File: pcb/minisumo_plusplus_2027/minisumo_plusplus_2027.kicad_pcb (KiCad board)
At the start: 2 copper layers, 45 x 33 mm, 13 parts, among them J1 IR - Conn_01x03_Pin, J2 IR - Conn_01x03_Pin, J3 Start Module - Conn_01x04_Pin, J4 US - Conn_01x04_Pin, SW1 SW_SPDT, U3 ESP32-C6-SuperMini

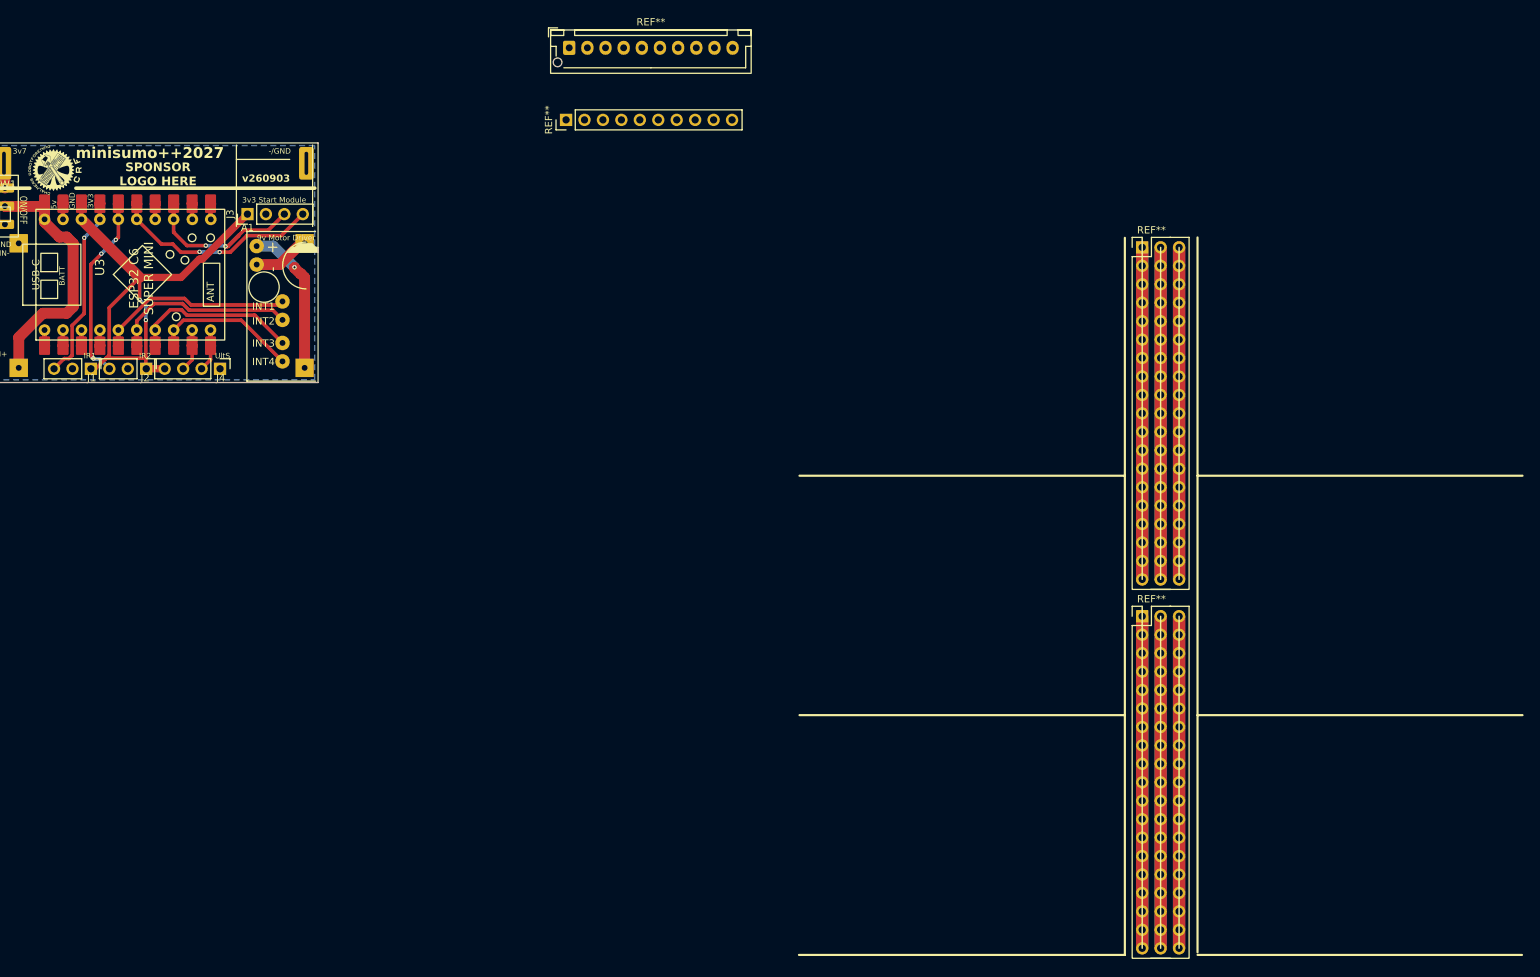
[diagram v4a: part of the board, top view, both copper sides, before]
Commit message: pcb - 1x10 for ir front/back and ultrasonic instead of 2x 1x3 + 1x4 && also included a 6x fab board example of latest board
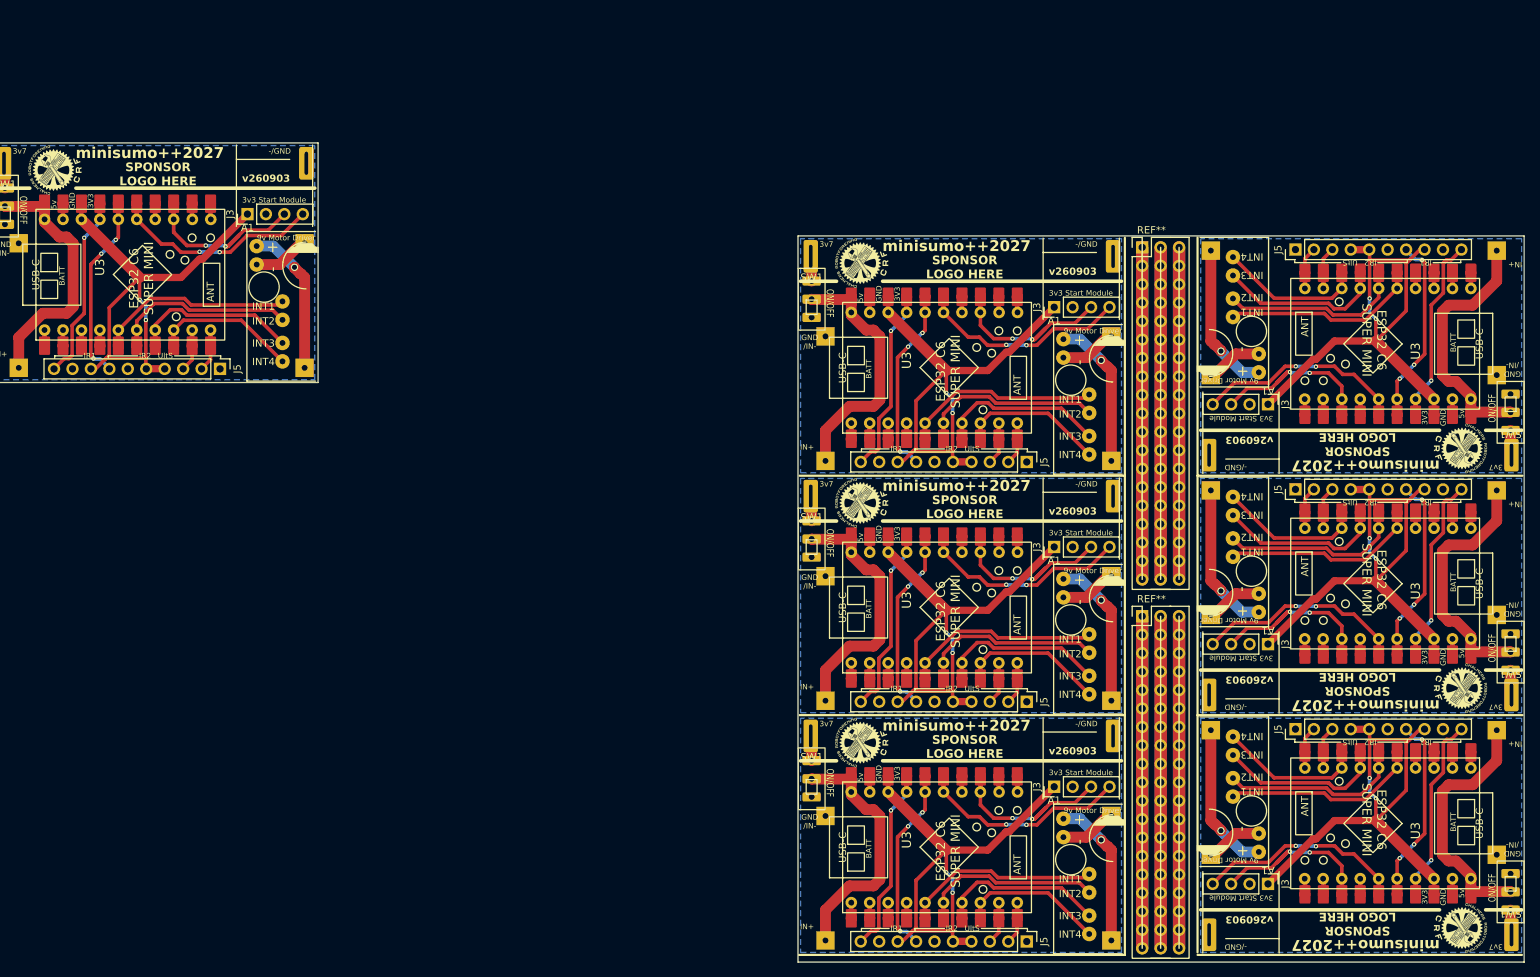
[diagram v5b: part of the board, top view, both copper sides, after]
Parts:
- removed J1, J2: IR - Conn_01x03_Pin, Connector_PinHeader_2.54mm:PinHeader_1x03_P2.54mm_Vertical
- removed J4: US - Conn_01x04_Pin, Connector_PinHeader_2.54mm:PinHeader_1x04_P2.54mm_Vertical
- removed the REF** at (108.4, 22.1)
- removed the REF** at (108.0, 32.0)
- added A1: ~, minisumo_plusplus_2027:Mini_L298N_2_Channel_H_Bridge_DC_Motor_Driver_Board_with_MX1508-special_silk, F.Cu at (175.2, 60.2)
- added A1: ~, minisumo_plusplus_2027:Mini_L298N_2_Channel_H_Bridge_DC_Motor_Driver_Board_with_MX1508-special_silk, F.Cu at (204.7, 101.8)
- added A1: ~, minisumo_plusplus_2027:Mini_L298N_2_Channel_H_Bridge_DC_Motor_Driver_Board_with_MX1508-special_silk, F.Cu at (175.2, 126.2)
- added A1: ~, minisumo_plusplus_2027:Mini_L298N_2_Channel_H_Bridge_DC_Motor_Driver_Board_with_MX1508-special_silk, F.Cu at (175.2, 93.2)
- added A1: ~, minisumo_plusplus_2027:Mini_L298N_2_Channel_H_Bridge_DC_Motor_Driver_Board_with_MX1508-special_silk, F.Cu at (204.7, 134.9)
- added A1: ~, minisumo_plusplus_2027:Mini_L298N_2_Channel_H_Bridge_DC_Motor_Driver_Board_with_MX1508-special_silk, F.Cu at (204.7, 68.8)
- added A2: ~, minisumo_plusplus_2027:XL6009 4A Boost Converter Step Up Adjustable 15W 5-32V to 5-50V DC-DC Power Supply Module LM2577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, B.Cu at (238.1, 81.1)
- added A2: ~, minisumo_plusplus_2027:XL6009 4A Boost Converter Step Up Adjustable 15W 5-32V to 5-50V DC-DC Power Supply Module LM2577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, B.Cu at (141.8, 80.9)
- added A2: ~, minisumo_plusplus_2027:XL6009 4A Boost Converter Step Up Adjustable 15W 5-32V to 5-50V DC-DC Power Supply Module LM2577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, B.Cu at (238.1, 48.1)
- added A2: ~, minisumo_plusplus_2027:XL6009 4A Boost Converter Step Up Adjustable 15W 5-32V to 5-50V DC-DC Power Supply Module LM2577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, B.Cu at (238.1, 114.2)
- added A2: ~, minisumo_plusplus_2027:XL6009 4A Boost Converter Step Up Adjustable 15W 5-32V to 5-50V DC-DC Power Supply Module LM2577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, B.Cu at (141.8, 146.9)
- added A2: ~, minisumo_plusplus_2027:XL6009 4A Boost Converter Step Up Adjustable 15W 5-32V to 5-50V DC-DC Power Supply Module LM2577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, B.Cu at (141.8, 113.9)
- added J3: Start Module - Conn_01x04_Pin, Connector_PinHeader_2.54mm:PinHeader_1x04_P2.54mm_Vertical, F.Cu at (204.7, 137.2)
- added J3: Start Module - Conn_01x04_Pin, Connector_PinHeader_2.54mm:PinHeader_1x04_P2.54mm_Vertical, F.Cu at (204.7, 104.2)
- added J3: Start Module - Conn_01x04_Pin, Connector_PinHeader_2.54mm:PinHeader_1x04_P2.54mm_Vertical, F.Cu at (204.7, 71.2)
- added J3: Start Module - Conn_01x04_Pin, Connector_PinHeader_2.54mm:PinHeader_1x04_P2.54mm_Vertical, F.Cu at (175.2, 123.9)
- added J3: Start Module - Conn_01x04_Pin, Connector_PinHeader_2.54mm:PinHeader_1x04_P2.54mm_Vertical, F.Cu at (175.2, 90.8)
- added J3: Start Module - Conn_01x04_Pin, Connector_PinHeader_2.54mm:PinHeader_1x04_P2.54mm_Vertical, F.Cu at (175.2, 57.8)
- added J5: Conn_01x10_Pin, Connector_PinHeader_2.54mm:PinHeader_1x10_P2.54mm_Vertical, F.Cu at (171.5, 112.1)
- added J5: Conn_01x10_Pin, Connector_PinHeader_2.54mm:PinHeader_1x10_P2.54mm_Vertical, F.Cu at (171.5, 79.1)
- added J5: Conn_01x10_Pin, Connector_PinHeader_2.54mm:PinHeader_1x10_P2.54mm_Vertical, F.Cu at (208.5, 49.9)
- added J5: Conn_01x10_Pin, Connector_PinHeader_2.54mm:PinHeader_1x10_P2.54mm_Vertical, F.Cu at (208.5, 115.9)
- added J5: Conn_01x10_Pin, Connector_PinHeader_2.54mm:PinHeader_1x10_P2.54mm_Vertical, F.Cu at (208.5, 82.9)
- added J5: Conn_01x10_Pin, Connector_PinHeader_2.54mm:PinHeader_1x10_P2.54mm_Vertical, F.Cu at (60.4, 66.3)
- added J5: Conn_01x10_Pin, Connector_PinHeader_2.54mm:PinHeader_1x10_P2.54mm_Vertical, F.Cu at (171.5, 145.2)
- added SW1: SW_SPDT, minisumo_plusplus_2027:SPST_switch_SS-12D00G4_1P2T_2.5mm_pitch_vert, F.Cu at (238.1, 74.8)
- added SW1: SW_SPDT, minisumo_plusplus_2027:SPST_switch_SS-12D00G4_1P2T_2.5mm_pitch_vert, F.Cu at (141.8, 87.2)
- added SW1: SW_SPDT, minisumo_plusplus_2027:SPST_switch_SS-12D00G4_1P2T_2.5mm_pitch_vert, F.Cu at (141.8, 54.2)
- added SW1: SW_SPDT, minisumo_plusplus_2027:SPST_switch_SS-12D00G4_1P2T_2.5mm_pitch_vert, F.Cu at (238.1, 140.8)
- added SW1: SW_SPDT, minisumo_plusplus_2027:SPST_switch_SS-12D00G4_1P2T_2.5mm_pitch_vert, F.Cu at (238.1, 107.8)
- added SW1: SW_SPDT, minisumo_plusplus_2027:SPST_switch_SS-12D00G4_1P2T_2.5mm_pitch_vert, F.Cu at (141.8, 120.3)
- added U2: ~, minisumo_plusplus_2027:battery cr123 3.7v with contacts for 18650_special_silk, B.Cu at (238.2, 78.2)
- added U2: ~, minisumo_plusplus_2027:battery cr123 3.7v with contacts for 18650_special_silk, B.Cu at (238.2, 111.2)
- added U2: ~, minisumo_plusplus_2027:battery cr123 3.7v with contacts for 18650_special_silk, B.Cu at (141.7, 83.8)
- added U2: ~, minisumo_plusplus_2027:battery cr123 3.7v with contacts for 18650_special_silk, B.Cu at (141.7, 50.8)
- added U2: ~, minisumo_plusplus_2027:battery cr123 3.7v with contacts for 18650_special_silk, B.Cu at (238.2, 144.2)
- added U2: ~, minisumo_plusplus_2027:battery cr123 3.7v with contacts for 18650_special_silk, B.Cu at (141.7, 116.9)
- added U3: ESP32-C6-SuperMini, minisumo_plusplus_2027:ESP32-C6-SuperMini_SMD_THT, F.Cu at (232.6, 137.5)
- added U3: ESP32-C6-SuperMini, minisumo_plusplus_2027:ESP32-C6-SuperMini_SMD_THT, F.Cu at (232.6, 104.5)
- added U3: ESP32-C6-SuperMini, minisumo_plusplus_2027:ESP32-C6-SuperMini_SMD_THT, F.Cu at (147.3, 123.6)
- added U3: ESP32-C6-SuperMini, minisumo_plusplus_2027:ESP32-C6-SuperMini_SMD_THT, F.Cu at (232.6, 71.5)
- added U3: ESP32-C6-SuperMini, minisumo_plusplus_2027:ESP32-C6-SuperMini_SMD_THT, F.Cu at (147.3, 90.5)
- added U3: ESP32-C6-SuperMini, minisumo_plusplus_2027:ESP32-C6-SuperMini_SMD_THT, F.Cu at (147.3, 57.5)
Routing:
- net 3v3: track 66.5 -> 465.5 mm, vias 2 -> 14
- net /3v7 (>3v3 & <5v): track 35.5 -> 248.5 mm
- net START Kill - not mandatory for sumo: track 29.1 -> 203.8 mm, vias 2 -> 14
- net IR Rear: track 28.2 -> 197.6 mm, vias 3 -> 21
- net START Start: track 26.7 -> 187.2 mm, vias 2 -> 14
- net Net-(A1-INT1): track 26.6 -> 186.0 mm
- net Net-(A1-INT2): track 25.4 -> 177.8 mm
- net IR Front: track 25.3 -> 177.4 mm, vias 1 -> 7
- net Net-(A1-INT3): track 23.2 -> 162.1 mm
- net /9v: track 20.9 -> 146.2 mm, vias 1 -> 7
- net Net-(A1-INT4): track 20.0 -> 140.3 mm
- net Net-(A1-gnd): track 7.31 -> 51.2 mm
- net US Echo Tx: track 5.85 -> 40.9 mm
- net US Trigger Rx: track 5.85 -> 40.9 mm
- net Net-(SW1-A): track 3.27 -> 22.9 mm
- added copper zone on B.Cu, net GND
- removed copper zone on B.Cu, net (none)
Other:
- board size 45 x 33 mm -> 211.1 x 112.8 mm

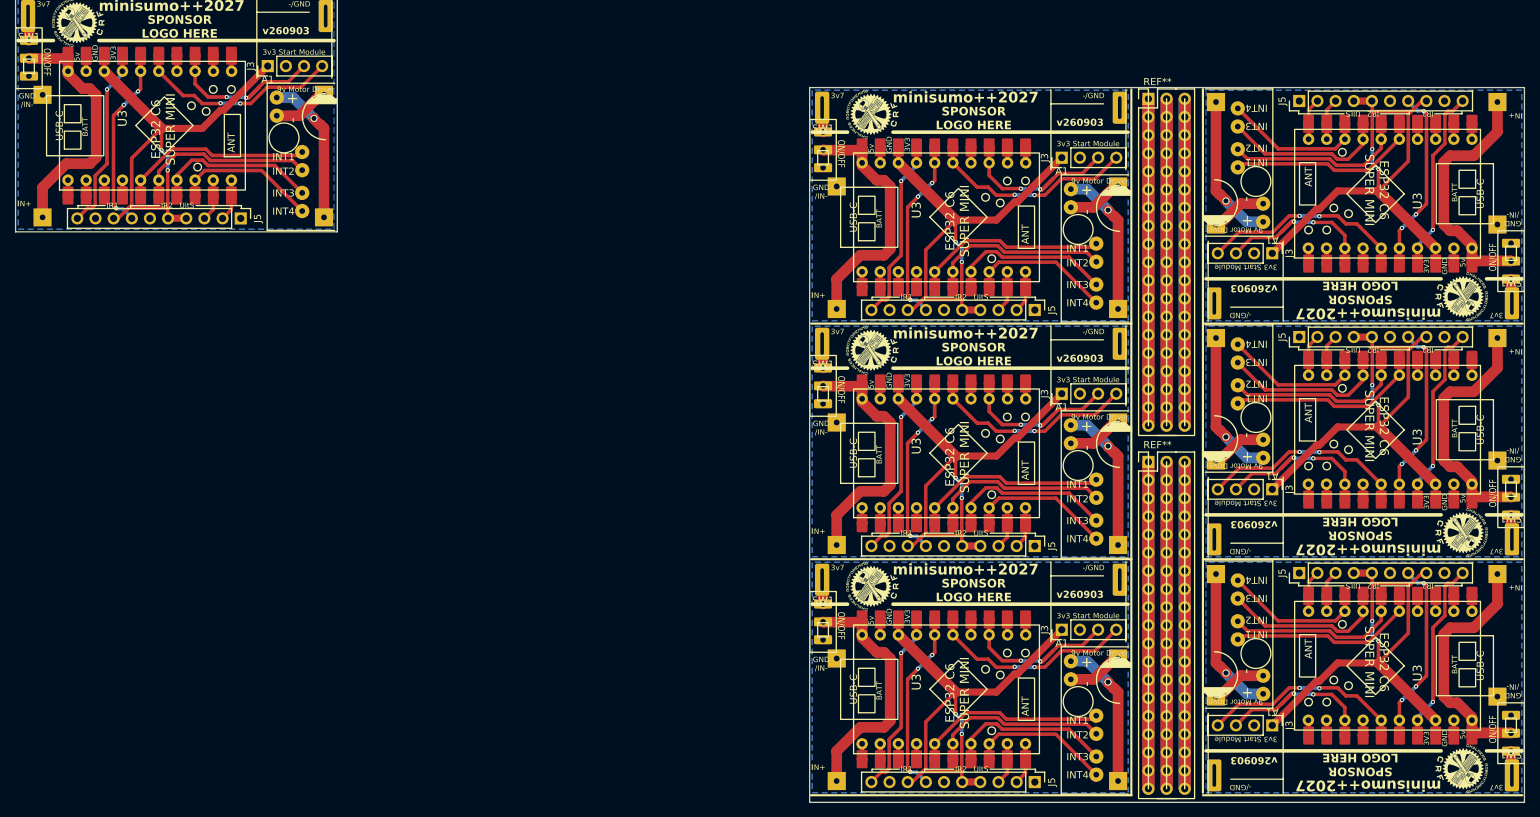
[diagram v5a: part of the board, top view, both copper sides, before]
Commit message: pcb - updated esp32 c6 footprint to match better && fixed traces based on some potential ANT issues leading to these improvements
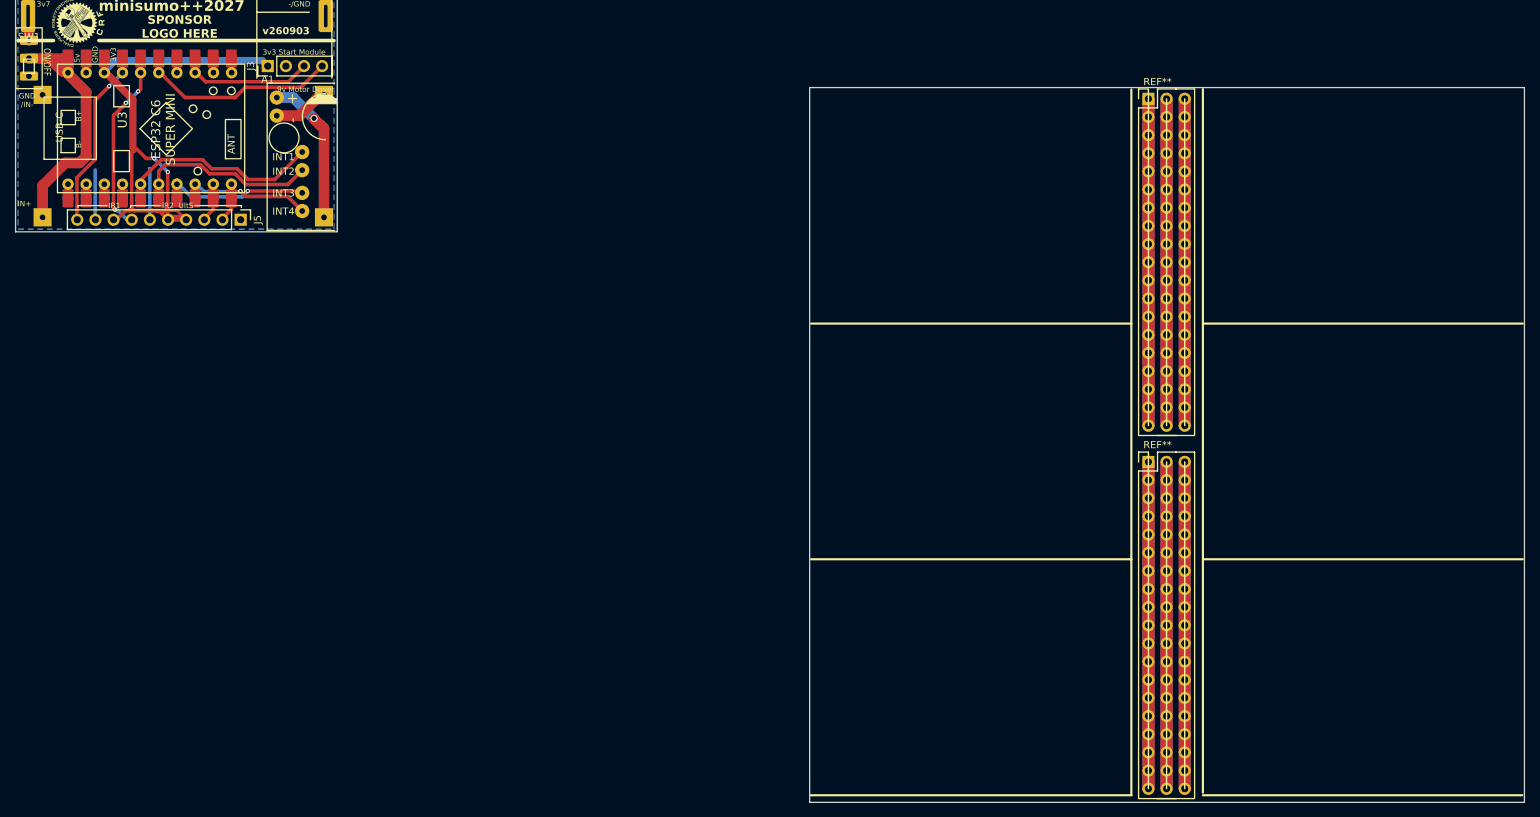
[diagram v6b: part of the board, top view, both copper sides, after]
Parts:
- removed the A1 at (175.2, 60.2)
- removed the A1 at (204.7, 101.8)
- removed the A1 at (175.2, 126.2)
- removed the A1 at (175.2, 93.2)
- removed the A1 at (204.7, 134.9)
- removed the A1 at (204.7, 68.8)
- removed the A2 at (238.1, 81.1)
- removed the A2 at (141.8, 80.9)
- removed the A2 at (238.1, 48.1)
- removed the A2 at (238.1, 114.2)
- removed the A2 at (141.8, 146.9)
- removed the A2 at (141.8, 113.9)
- removed the J3 at (204.7, 137.2)
- removed the J3 at (204.7, 104.2)
- removed the J3 at (204.7, 71.2)
- removed the J3 at (175.2, 123.9)
- removed the J3 at (175.2, 90.8)
- removed the J3 at (175.2, 57.8)
- removed the J5 at (171.5, 112.1)
- removed the J5 at (171.5, 79.1)
- removed the J5 at (208.5, 49.9)
- removed the J5 at (208.5, 115.9)
- removed the J5 at (208.5, 82.9)
- removed the J5 at (171.5, 145.2)
- removed the SW1 at (238.1, 74.8)
- removed the SW1 at (141.8, 87.2)
- removed the SW1 at (141.8, 54.2)
- removed the SW1 at (238.1, 140.8)
- removed the SW1 at (238.1, 107.8)
- removed the SW1 at (141.8, 120.3)
- removed the U2 at (238.2, 78.2)
- removed the U2 at (238.2, 111.2)
- removed the U2 at (141.7, 83.8)
- removed the U2 at (141.7, 50.8)
- removed the U2 at (238.2, 144.2)
- removed the U2 at (141.7, 116.9)
- removed the U3 at (232.6, 137.5)
- removed the U3 at (232.6, 104.5)
- removed the U3 at (147.3, 123.6)
- removed the U3 at (232.6, 71.5)
- removed the U3 at (147.3, 90.5)
- removed the U3 at (147.3, 57.5)
- moved U3 0.20 mm to (36.2, 44.9)
- moved J5 0.19 mm to (60.4, 66.5)
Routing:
- net 3v3: track 465.5 -> 75.5 mm, vias 14 -> 2
- net /3v7 (>3v3 & <5v): track 248.5 -> 36.3 mm
- net START Kill - not mandatory for sumo: track 203.8 -> 28.4 mm, vias 14 -> 0
- net IR Rear: track 197.6 -> 28.3 mm, vias 21 -> 3
- net START Start: track 187.2 -> 18.9 mm, vias 14 -> 0
- net Net-(A1-INT1): track 186.0 -> 28.1 mm
- net IR Front: track 177.4 -> 25.4 mm, vias 7 -> 1
- net Net-(A1-INT2): track 177.8 -> 25.8 mm
- net Net-(A1-INT3): track 162.1 -> 20.6 mm, vias 0 -> 1
- net /9v: track 146.2 -> 20.9 mm, vias 7 -> 1
- net Net-(A1-INT4): track 140.3 -> 18.6 mm, vias 0 -> 1
- net Net-(A1-gnd): track 51.2 -> 7.31 mm
- net US Echo Tx: track 40.9 -> 5.85 mm
- net US Trigger Rx: track 40.9 -> 5.85 mm
- net Net-(SW1-A): track 22.9 -> 3.27 mm
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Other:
- board text added: "BUCK BOOST LM2596"
